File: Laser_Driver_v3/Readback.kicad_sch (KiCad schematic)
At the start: 43 parts, among them J2 SMA Isolated Coax, J3 SMA Isolated Coax, U25 INA826, U26 INA826, U27 INA826, U28 INA826, U29 OPA2141AID

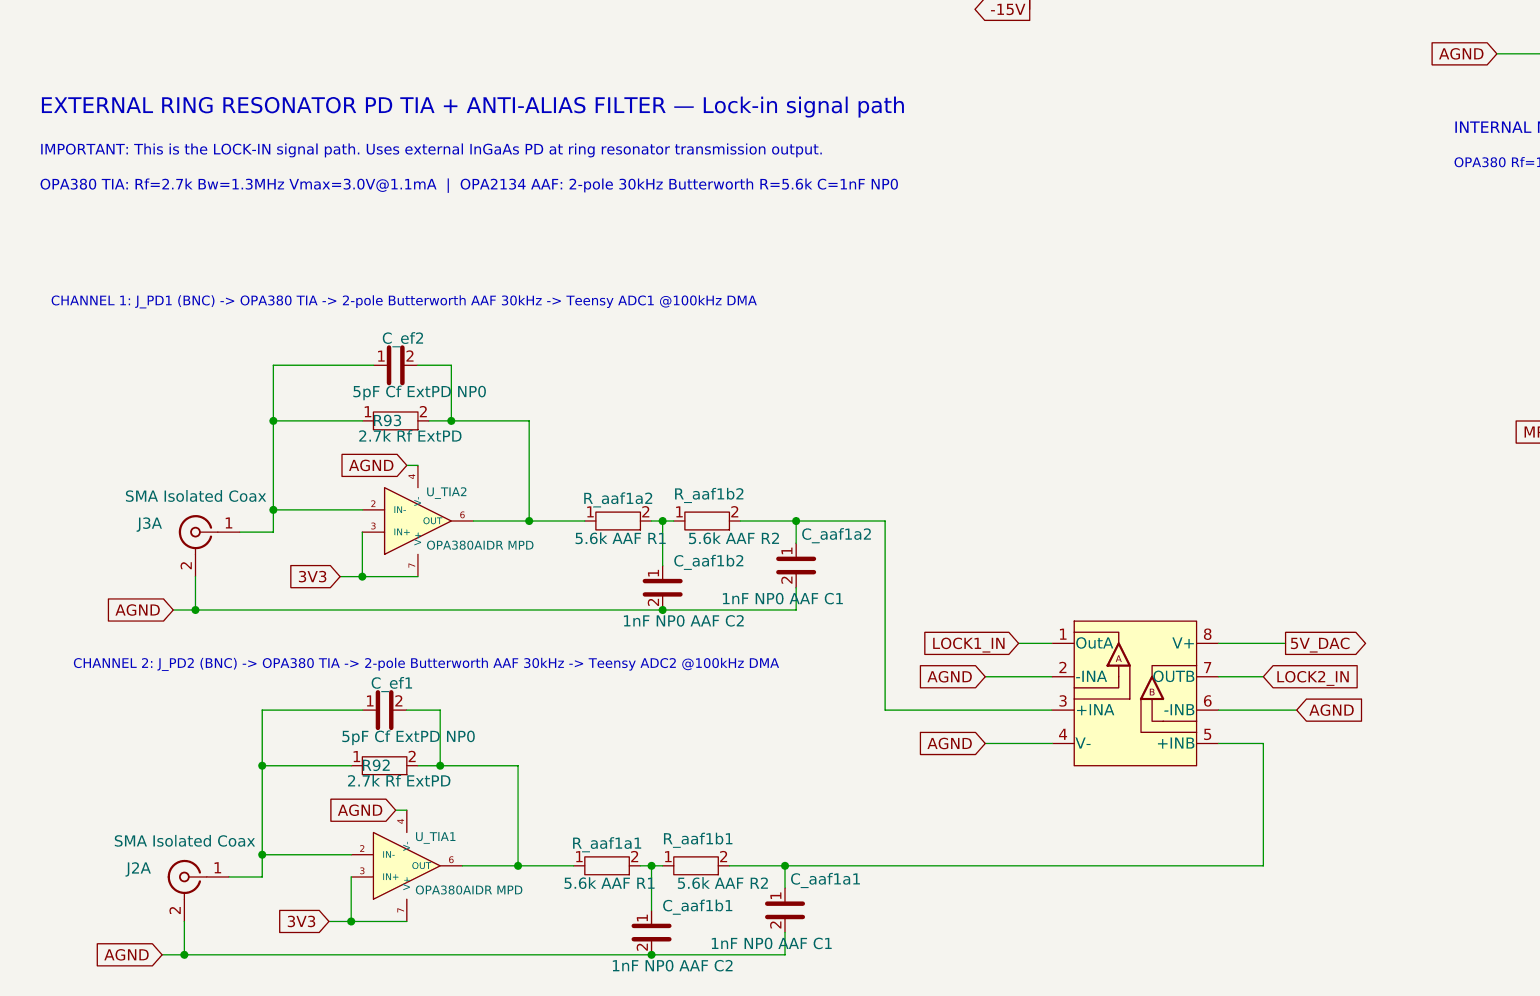
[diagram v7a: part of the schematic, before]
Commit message: Changed to an RF modulation
Based on the uncertainty calculation, needed to change from a low frequency modulation to an RF modulation.  This drive down the noise, but required a very different implentation.  The modulation is limited to about 2 MHz.  Much faster is at the limit of this hardware and would require significant increase in complexity and cost.
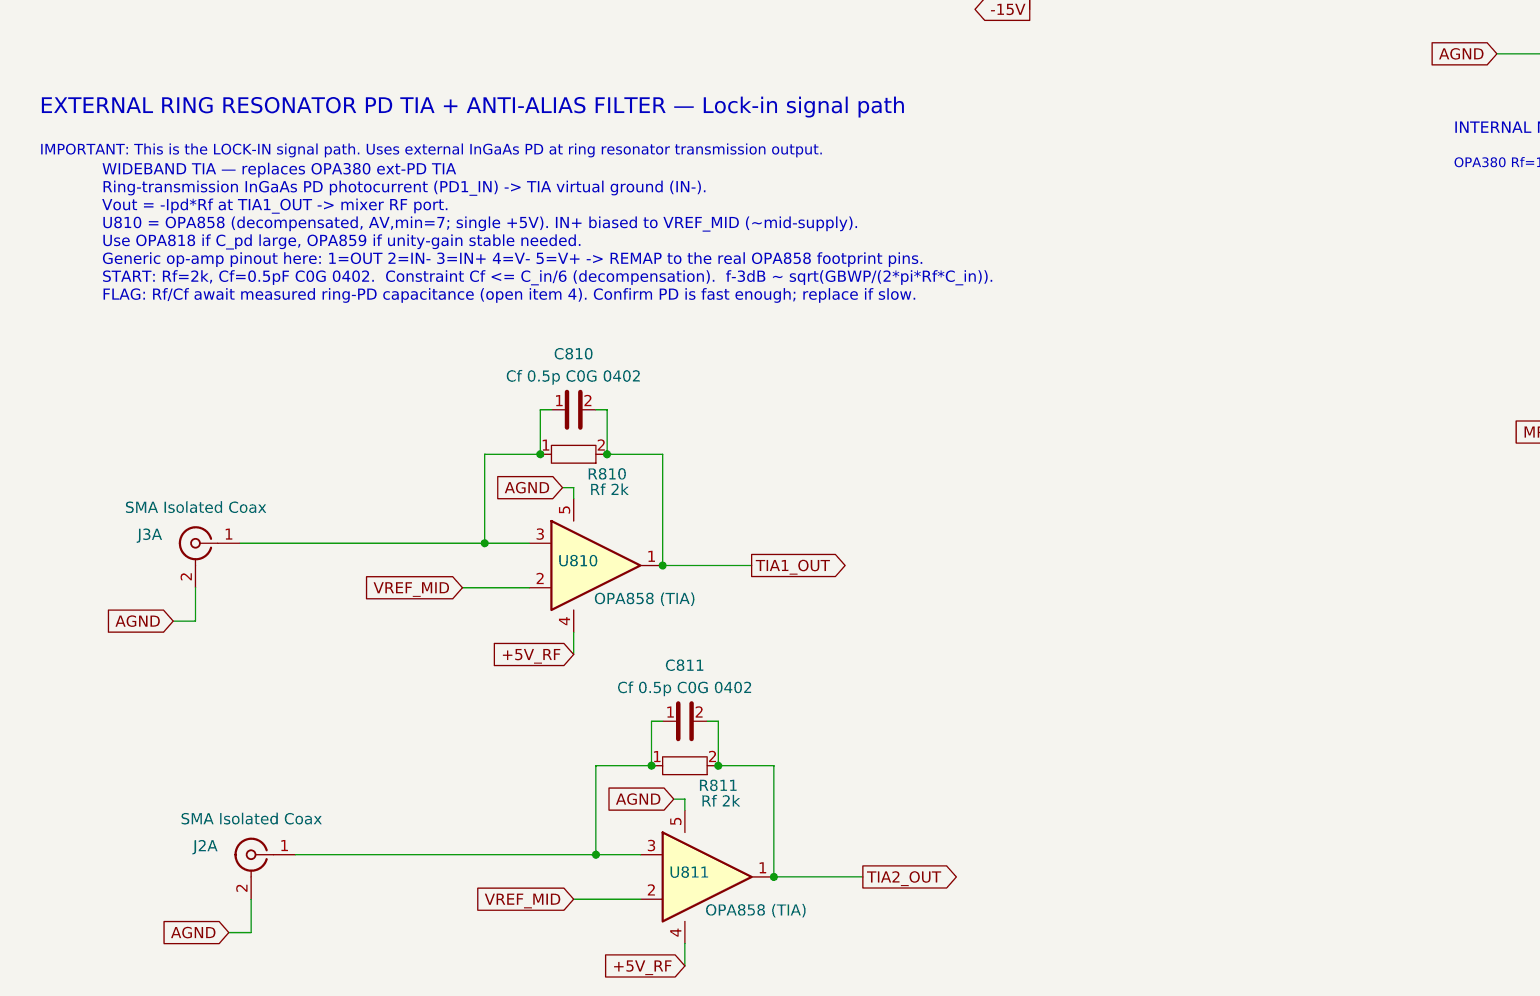
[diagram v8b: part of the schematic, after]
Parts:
- removed C_aaf1a1, C_aaf1a2: 1nF NP0 AAF C1, Capacitor_SMD:C_0805_2012Metric_Pad1.18x1.45mm_HandSolder, symbol Device:C
- removed C_aaf1b1, C_aaf1b2: 1nF NP0 AAF C2, Capacitor_SMD:C_0805_2012Metric_Pad1.18x1.45mm_HandSolder, symbol Device:C
- removed C_ef1, C_ef2: 5pF Cf ExtPD NP0, Capacitor_SMD:C_0402_1005Metric, symbol Device:C
- removed R92, R93: 2.7k Rf ExtPD, Resistor_SMD:R_0805_2012Metric_Pad1.20x1.40mm_HandSolder, symbol Device:R
- removed R_aaf1a1, R_aaf1a2: 5.6k AAF R1, Resistor_SMD:R_0805_2012Metric_Pad1.20x1.40mm_HandSolder, symbol Device:R
- removed R_aaf1b1, R_aaf1b2: 5.6k AAF R2, Resistor_SMD:R_0805_2012Metric_Pad1.20x1.40mm_HandSolder, symbol Device:R
- removed U29: OPA2141AID, Package_SO:SOIC-8_3.9x4.9mm_P1.27mm, symbol Amplifier_Operational:OPA2134
- removed U_TIA1, U_TIA2: OPA380AIDR MPD, Package_SO:SOIC-8_3.9x4.9mm_P1.27mm, symbol Amplifier_Operational:OPA380
- added C810, C811: Cf 0.5p C0G 0402, symbol Device:C
- added R810, R811: Rf 2k, symbol Device:R
- added U810, U811: OPA858 (TIA), symbol RFblk:OpAmp
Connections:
- net AGND: now also U810.5 (V+), U811.5 (V+)
- net at J2.1 (In1): now also C811.1, R811.1, U811.3 (+)
- net at J3.1 (In1): now also C810.1, R810.1, U810.3 (+)
- new net +5V_RF: U810.4 (V-), U811.4 (V-)
- new net TIA1_OUT: C810.2, R810.2, U810.1 (OUT)
- new net TIA2_OUT: C811.2, R811.2, U811.1 (OUT)
- new net VREF_MID: U810.2 (-), U811.2 (-)
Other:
- note added: "WIDEBAND TIA — replaces OPA380 ext-PD TIA Ring-transmission InGaAs PD photocurrent (PD1_IN) -> TIA virtual ground (IN-). Vout = -Ipd*Rf at TIA1_OUT -> mixer RF port. U810 = OPA858 (decompensated, AV,min=7; single +5V). IN+ biased to VREF_MID (~mid-supply). Use OPA818 if C_pd large, OPA859 if unity-gain stable needed. Generic op-amp pinout here: 1=OUT 2=IN- 3=IN+ 4=V- 5=V+ -> REMAP to the real OPA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"
- note removed: "CHANNEL 1: J_PD1 (BNC) -> OPA380 TIA -> 2-pole Butterworth AAF 30kHz -> Teensy ADC1 @100kHz DMA"
- note removed: "CHANNEL 2: J_PD2 (BNC) -> OPA380 TIA -> 2-pole Butterworth AAF 30kHz -> Teensy ADC2 @100kHz DMA"
- note removed: "OPA380 TIA: Rf=2.7k Bw=1.3MHz Vmax=3.0V@1.1mA | OPA2134 AAF: 2-pole 30kHz Butterworth R=5.6k C=1nF NP0"
- moved on the sheet: J2A, J3A
